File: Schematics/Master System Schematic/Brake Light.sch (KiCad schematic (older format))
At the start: 3 parts, among them U10 KY-019, U13 CAN_Bus_Module

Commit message: Cooling Pump, TSMP container Updates
>Added Cooling pump relay
>Added Cooling pump
>Added +12V plug to TSMP container
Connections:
- new net: A2.~ (~~D9), U13.~ (Serial_Clock) (x6)
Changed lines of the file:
@@
 EESchema Schematic File Version 4
-LIBS:Master System Schematic-cache
 EELAYER 30 0
 EELAYER END

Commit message: Started Voltage tap pcbs
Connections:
- new net: A2.~ (~~D9), U13.~ (Serial_Clock) (x6)
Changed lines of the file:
@@
 $Descr A4 11693 8268
 encoding utf-8
-Sheet 13 13
+Sheet 13 17
 Title ""
 Date "2020-10-12"

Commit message: Fixed CAN
Changed to represent one connection. This ofc can be changed back if you meant to imply two CAN connections coming in
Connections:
- new net: A2.~ (~~D9), U13.~ (Serial_Clock) (x6)
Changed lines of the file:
@@
 EESchema Schematic File Version 4
+LIBS:Master System Schematic-cache
 EELAYER 30 0
 EELAYER END

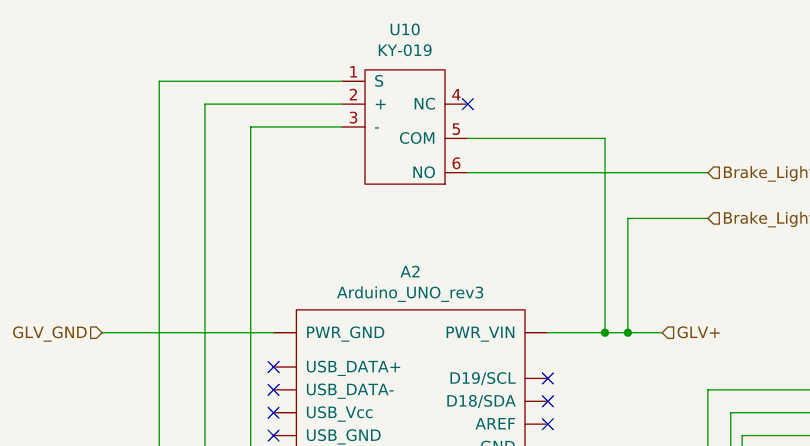
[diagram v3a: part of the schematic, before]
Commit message: Had to refactor all IDs
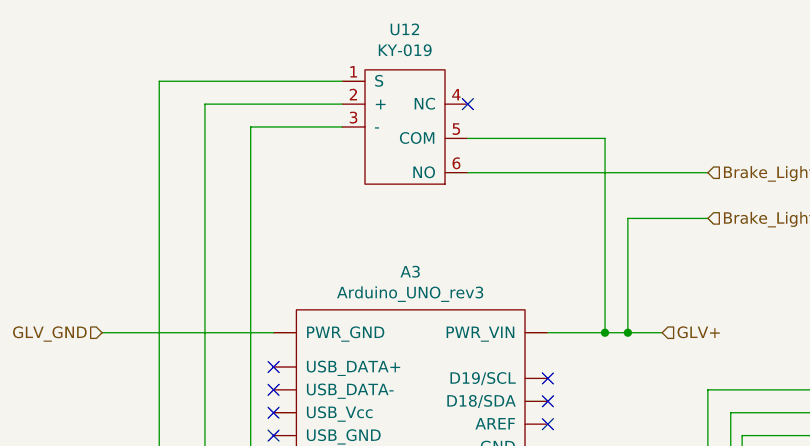
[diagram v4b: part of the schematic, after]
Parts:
- renumbered A2 to A3, U10 to U12
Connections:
- new net: A3.~ (~~D9), U13.~ (Serial_Clock) (x6)
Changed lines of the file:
@@
 $Descr A4 11693 8268
 encoding utf-8
-Sheet 13 17
+Sheet 13 21
 Title ""
 Date "2020-10-12"
@@
 $EndDescr
 $Comp
-L NER:Arduino_UNO_rev3 A2
+L NER:Arduino_UNO_rev3 A3
 U 1 1 5F8BEBC7
 P 4700 2700
-F 0 "A2" H 4700 2815 50  0000 C CNN
+F 0 "A3" H 4700 2815 50  0000 C CNN
 F 1 "Arduino_UNO_rev3" H 4700 2724 50  0000 C CNN
 F 2 "" H 4700 2850 50  0001 C CNN
@@
 $EndComp
 $Comp
-L NER:KY-019 U10
+L NER:KY-019 U12
 U 1 1 5F8C06C7
 P 4700 1950
-F 0 "U10" V 4275 1925 50  0000 C CNN
+F 0 "U12" V 4275 1925 50  0000 C CNN
 F 1 "KY-019" V 4366 1925 50  0000 C CNN
 F 2 "" H 4650 1650 50  0001 C CNN

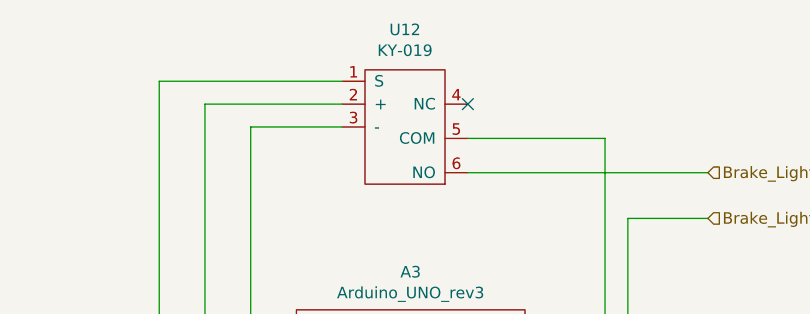
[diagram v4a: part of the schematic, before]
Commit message: Fixed Driver IO and annotations
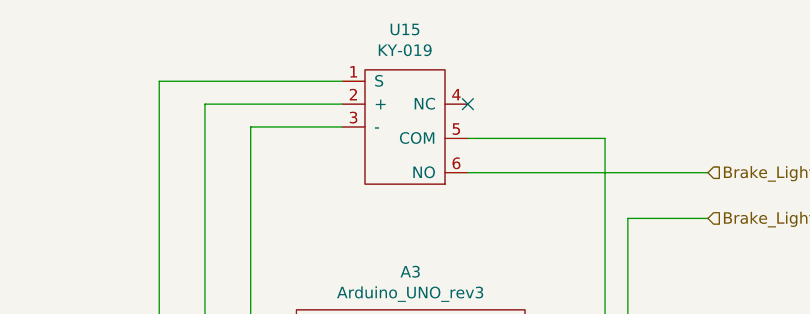
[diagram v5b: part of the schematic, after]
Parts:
- renumbered U12 to U15
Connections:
- new net: A3.~ (~~D9), U13.~ (Serial_Clock) (x6)
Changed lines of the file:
@@
 EESchema Schematic File Version 4
-LIBS:Master System Schematic-cache
 EELAYER 30 0
 EELAYER END
 $Descr A4 11693 8268
 encoding utf-8
-Sheet 13 21
+Sheet 21 21
 Title ""
 Date "2020-10-12"
@@
 $EndComp
 $Comp
-L NER:KY-019 U12
+L NER:KY-019 U15
 U 1 1 5F8C06C7
 P 4700 1950
-F 0 "U12" V 4275 1925 50  0000 C CNN
+F 0 "U15" V 4275 1925 50  0000 C CNN
 F 1 "KY-019" V 4366 1925 50  0000 C CNN
 F 2 "" H 4650 1650 50  0001 C CNN

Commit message: Added Master Schematic Wiring
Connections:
- new net: A3.~ (~~D9), U13.~ (Serial_Clock) (x6)
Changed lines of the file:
@@
 EESchema Schematic File Version 4
+LIBS:Master System Schematic-cache
 EELAYER 30 0
 EELAYER END

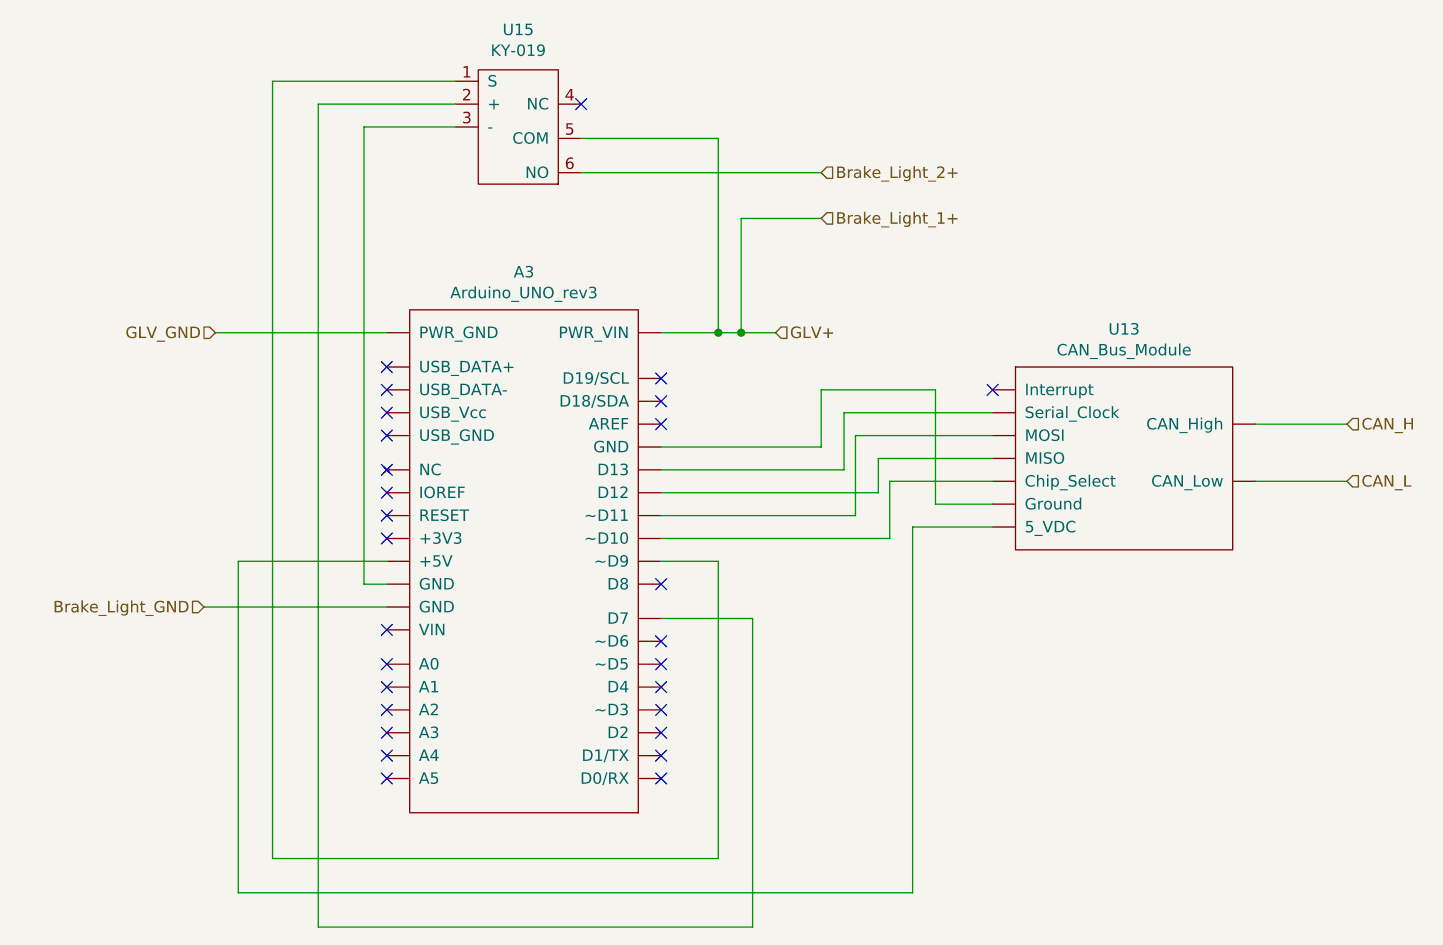
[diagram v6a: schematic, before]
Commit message: Cleaned up/Finalized Driver IO Schematic
Added a 100 ohm resistor to the 3v button to drop the 5v from the arduino to 3v. Cleaned up the messy wires.
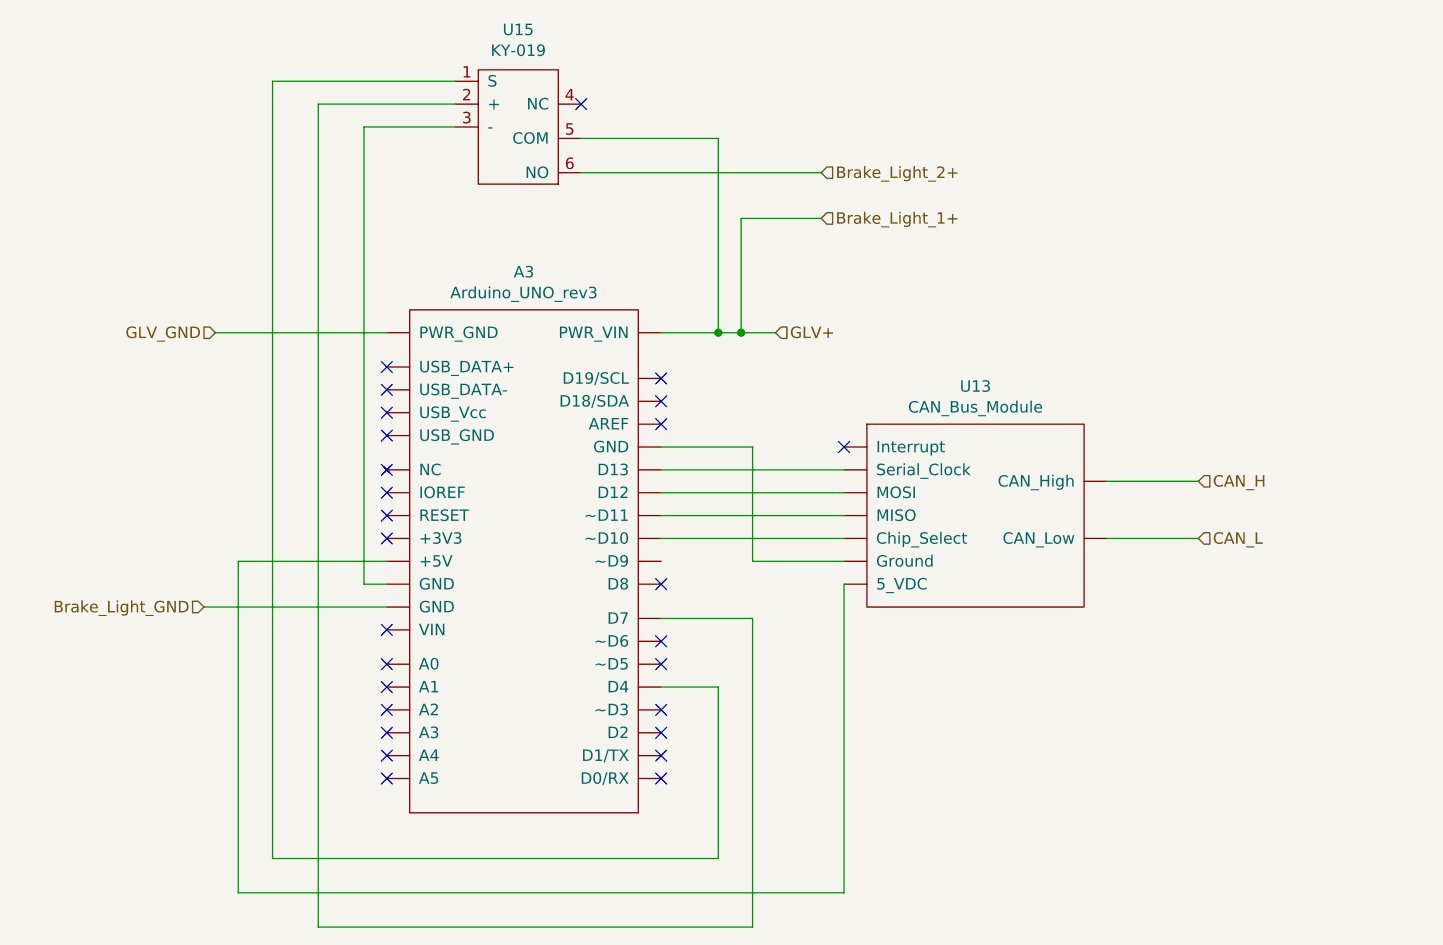
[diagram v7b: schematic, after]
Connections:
- new net: A3.~ (~~D9), U13.~ (Serial_Clock) (x6)
- no-connect marks 28 -> 27
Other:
- moved on the sheet: U13
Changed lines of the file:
@@
 EESchema Schematic File Version 4
-LIBS:Master System Schematic-cache
 EELAYER 30 0
 EELAYER END
@@
 L NER:CAN_Bus_Module U13
 U 1 1 5F8C522E
-P 7300 2950
-F 0 "U13" H 7325 3065 50  0000 C CNN
-F 1 "CAN_Bus_Module" H 7325 2974 50  0000 C CNN
-F 2 "" H 7300 2950 50  0001 C CNN
-F 3 "" H 7300 2950 50  0001 C CNN
-	1    7300 2950
+P 6650 3200
+F 0 "U13" H 6675 3315 50  0000 C CNN
+F 1 "CAN_Bus_Module" H 6675 3224 50  0000 C CNN
+F 2 "" H 6650 3200 50  0001 C CNN
+F 3 "" H 6650 3200 50  0001 C CNN
+	1    6650 3200
 	1    0    0    -1
 $EndComp
-NoConn ~ 6750 3100
-Wire Wire Line
-	6750 3200 6100 3200
-Wire Wire Line
-	6100 3200 6100 3450
-Wire Wire Line
-	6100 3450 5300 3450
-Wire Wire Line
-	6750 3300 6150 3300
-Wire Wire Line
-	6150 3300 6150 3650
-Wire Wire Line
-	6150 3650 5300 3650
-Wire Wire Line
-	6750 3400 6250 3400
-Wire Wire Line
-	6250 3400 6250 3550
-Wire Wire Line
-	6250 3550 5300 3550
-Wire Wire Line
-	6750 3700 6400 3700
-Wire Wire Line
-	6400 3700 6400 5300
-Wire Wire Line
-	6400 5300 3450 5300
+NoConn ~ 6100 3350
 Wire Wire Line
 	3450 5300 3450 3850
 Wire Wire Line
 	3450 3850 4100 3850
-Wire Wire Line
-	6750 3500 6300 3500
-Wire Wire Line
-	6300 3500 6300 3750
-Wire Wire Line
-	6300 3750 5300 3750
-Wire Wire Line
-	6750 3600 6500 3600
-Wire Wire Line
-	6500 3600 6500 3100
-Wire Wire Line
-	6500 3100 6000 3100
-Wire Wire Line
-	6000 3100 6000 3350
-Wire Wire Line
-	6000 3350 5300 3350
-Text HLabel 8300 3250 2    50   Input ~ 0
+Text HLabel 7650 3500 2    50   Input ~ 0
 CAN_H
-Text HLabel 8300 3500 2    50   Input ~ 0
+Text HLabel 7650 3750 2    50   Input ~ 0
 CAN_L
 Wire Wire Line
-	8300 3250 7900 3250
+	7650 3500 7250 3500
 Wire Wire Line
-	8300 3500 7900 3500
+	7650 3750 7250 3750
 Text HLabel 5800 2850 2    50   Input ~ 0
 GLV+
@@
 Wire Wire Line
 	3600 5150 5550 5150
-Wire Wire Line
-	5550 5150 5550 3850
-Wire Wire Line
-	5550 3850 5300 3850
 Text HLabel 6000 2350 2    50   Input ~ 0
 Brake_Light_1+
@@
 NoConn ~ 5300 4200
 NoConn ~ 5300 4300
-NoConn ~ 5300 4400
 NoConn ~ 5300 4500
 NoConn ~ 5300 4600
@@
 NoConn ~ 4100 3100
 NoConn ~ 4100 3000
+Wire Wire Line
+	5550 5150 5550 4400
+Wire Wire Line
+	5550 4400 5300 4400
+Wire Wire Line
+	6100 3450 5300 3450
+Wire Wire Line
+	6100 3550 5300 3550
+Wire Wire Line
+	6100 3650 5300 3650
+Wire Wire Line
+	6100 3750 5300 3750
+Wire Wire Line
+	6100 3850 5700 3850
+Wire Wire Line
+	5700 3850 5700 3350
+Wire Wire Line
+	5700 3350 5300 3350
+Wire Wire Line
+	3450 5300 6100 5300
+Wire Wire Line
+	6100 5300 6100 3950
 $EndSCHEMATC

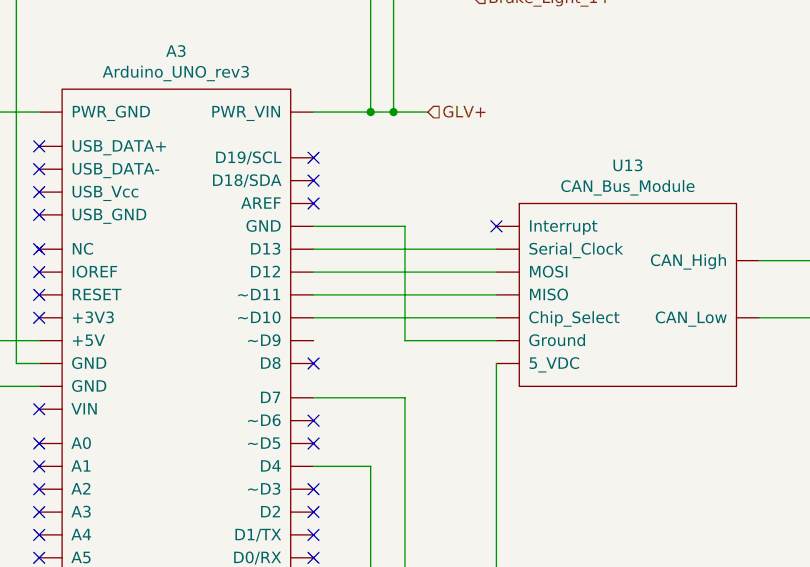
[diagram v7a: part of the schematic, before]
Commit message: Fixed Wiring on CAN Bus
I fixed the wiring on the CAN Bus in the brake light box that I messed up yesterday.
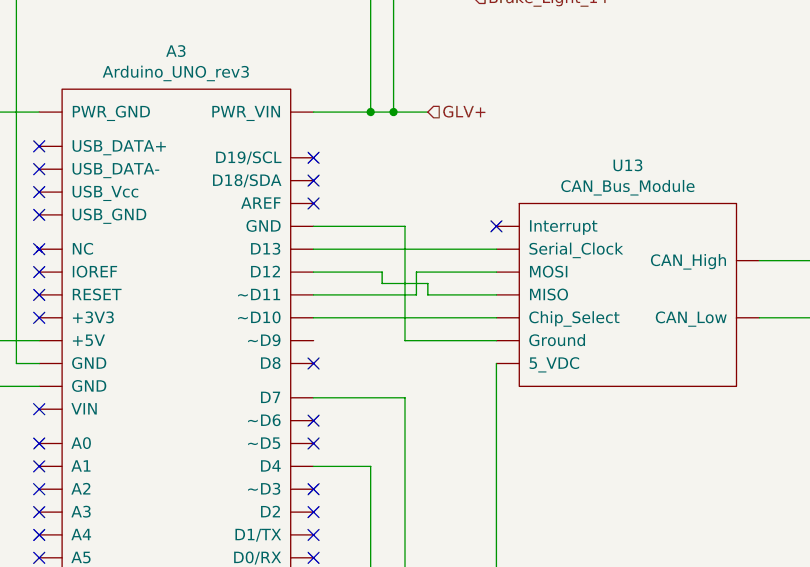
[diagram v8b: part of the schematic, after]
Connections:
- new net: A3.~ (~~D9), U13.~ (Serial_Clock) (x6)
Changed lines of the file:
@@
 $EndDescr
-$Comp
-L NER:Arduino_UNO_rev3 A3
-U 1 1 5F8BEBC7
-P 4700 2700
-F 0 "A3" H 4700 2815 50  0000 C CNN
-F 1 "Arduino_UNO_rev3" H 4700 2724 50  0000 C CNN
-F 2 "" H 4700 2850 50  0001 C CNN
-F 3 "" H 4700 2850 50  0001 C CNN
-	1    4700 2700
-	1    0    0    -1
-$EndComp
 $Comp
 L NER:KY-019 U15
@@
 	0    1    1    0
 $EndComp
-$Comp
-L NER:CAN_Bus_Module U13
-U 1 1 5F8C522E
-P 6650 3200
-F 0 "U13" H 6675 3315 50  0000 C CNN
-F 1 "CAN_Bus_Module" H 6675 3224 50  0000 C CNN
-F 2 "" H 6650 3200 50  0001 C CNN
-F 3 "" H 6650 3200 50  0001 C CNN
-	1    6650 3200
-	1    0    0    -1
-$EndComp
-NoConn ~ 6100 3350
 Wire Wire Line
 	3450 5300 3450 3850
-Wire Wire Line
-	3450 3850 4100 3850
 Text HLabel 7650 3500 2    50   Input ~ 0
 CAN_H
 Text HLabel 7650 3750 2    50   Input ~ 0
 CAN_L
-Wire Wire Line
-	7650 3500 7250 3500
-Wire Wire Line
-	7650 3750 7250 3750
 Text HLabel 5800 2850 2    50   Input ~ 0
 GLV+
@@
 GLV_GND
 Wire Wire Line
-	3350 2850 4100 2850
-Wire Wire Line
 	5550 2850 5550 2000
 Wire Wire Line
 	5550 2000 4950 2000
 Connection ~ 5550 2850
-Wire Wire Line
-	5550 2850 5300 2850
 Wire Wire Line
 	4400 1750 3600 1750
@@
 	5700 5450 5700 4100
 Wire Wire Line
-	5700 4100 5300 4100
-Wire Wire Line
 	4400 1950 4000 1950
 Wire Wire Line
 	4000 1950 4000 3950
-Wire Wire Line
-	4000 3950 4100 3950
 Wire Wire Line
 	5550 2850 5650 2850
@@
 Wire Wire Line
 	5650 2850 5800 2850
+NoConn ~ 4950 1850
 Wire Wire Line
-	4100 4050 3300 4050
-NoConn ~ 4950 1850
-NoConn ~ 5300 3050
-NoConn ~ 5300 3150
-NoConn ~ 5300 3250
-NoConn ~ 5300 3950
+	5550 5150 5550 4400
+Wire Wire Line
+	5700 3850 5700 3350
+Wire Wire Line
+	3450 5300 6100 5300
+NoConn ~ 6100 3350
+Wire Wire Line
+	6100 3850 5700 3850
+Wire Wire Line
+	7650 3750 7250 3750
+Wire Wire Line
+	7650 3500 7250 3500
+Wire Wire Line
+	6100 5300 6100 3950
 NoConn ~ 5300 4200
 NoConn ~ 5300 4300
 NoConn ~ 5300 4500
+Wire Wire Line
+	6100 3750 5300 3750
+NoConn ~ 4100 4150
+NoConn ~ 4100 3200
+NoConn ~ 4100 3300
+NoConn ~ 4100 3100
+NoConn ~ 4100 3000
+NoConn ~ 4100 3650
+Wire Wire Line
+	5550 2850 5300 2850
+Wire Wire Line
+	3350 2850 4100 2850
+NoConn ~ 4100 3450
+NoConn ~ 4100 3550
+Wire Wire Line
+	5700 3350 5300 3350
+Wire Wire Line
+	4000 3950 4100 3950
+Wire Wire Line
+	4100 4050 3300 4050
+NoConn ~ 5300 3950
+Wire Wire Line
+	5700 4100 5300 4100
+Wire Wire Line
+	5550 4400 5300 4400
 NoConn ~ 5300 4600
+NoConn ~ 5300 3050
+NoConn ~ 5300 3150
+Wire Wire Line
+	6100 3450 5300 3450
 NoConn ~ 5300 4700
 NoConn ~ 5300 4800
+NoConn ~ 5300 3250
 NoConn ~ 4100 4800
 NoConn ~ 4100 4700
@@
 NoConn ~ 4100 4400
 NoConn ~ 4100 4300
-NoConn ~ 4100 4150
+Wire Wire Line
+	3450 3850 4100 3850
 NoConn ~ 4100 3750
-NoConn ~ 4100 3650
-NoConn ~ 4100 3550
-NoConn ~ 4100 3450
-NoConn ~ 4100 3300
-NoConn ~ 4100 3200
-NoConn ~ 4100 3100
-NoConn ~ 4100 3000
+$Comp
+L NER:CAN_Bus_Module U13
+U 1 1 5F8C522E
+P 6650 3200
+F 0 "U13" H 6675 3315 50  0000 C CNN
+F 1 "CAN_Bus_Module" H 6675 3224 50  0000 C CNN
+F 2 "" H 6650 3200 50  0001 C CNN
+F 3 "" H 6650 3200 50  0001 C CNN
+	1    6650 3200
+	1    0    0    -1
+$EndComp
+$Comp
+L NER:Arduino_UNO_rev3 A3
+U 1 1 5F8BEBC7
+P 4700 2700
+F 0 "A3" H 4700 2815 50  0000 C CNN
+F 1 "Arduino_UNO_rev3" H 4700 2724 50  0000 C CNN
+F 2 "" H 4700 2850 50  0001 C CNN
+F 3 "" H 4700 2850 50  0001 C CNN
+	1    4700 2700
+	1    0    0    -1
+$EndComp
 Wire Wire Line
-	5550 5150 5550 4400
+	5300 3550 5600 3550
 Wire Wire Line
-	5550 4400 5300 4400
+	5600 3550 5600 3600
 Wire Wire Line
-	6100 3450 5300 3450
+	5800 3600 5800 3650
 Wire Wire Line
-	6100 3550 5300 3550
+	5800 3650 6100 3650
 Wire Wire Line
-	6100 3650 5300 3650
+	5600 3600 5800 3600
 Wire Wire Line
-	6100 3750 5300 3750
+	5750 3550 5750 3650
 Wire Wire Line
-	6100 3850 5700 3850
+	5750 3650 5300 3650
 Wire Wire Line
-	5700 3850 5700 3350
-Wire Wire Line
-	5700 3350 5300 3350
-Wire Wire Line
-	3450 5300 6100 5300
-Wire Wire Line
-	6100 5300 6100 3950
+	5750 3550 6100 3550
 $EndSCHEMATC
